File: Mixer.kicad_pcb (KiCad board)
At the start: 2 copper layers, 30 x 101 mm, 18 parts, among them J101 AudioJack2, J102 AudioJack2, J103 AudioJack2, J104 AudioJack2, J105 Conn_02x05_Counter_Clockwise, U101 TL072

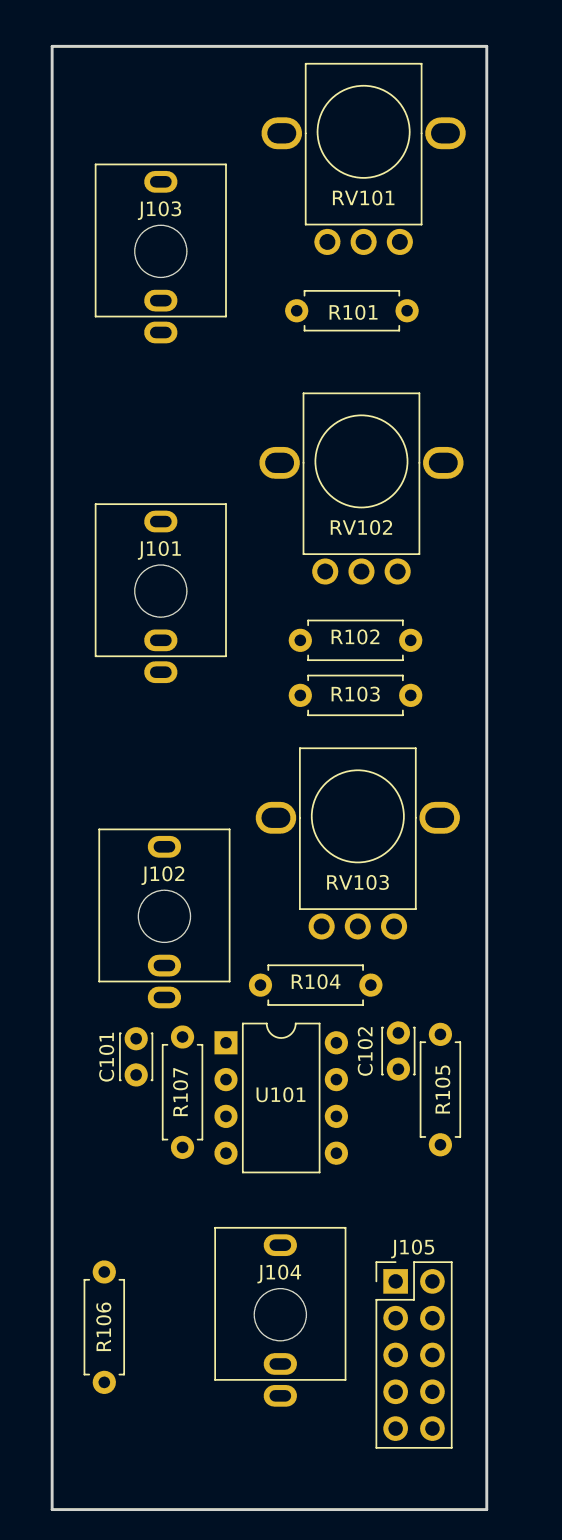
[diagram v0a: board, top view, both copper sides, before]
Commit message: Added attenuverters
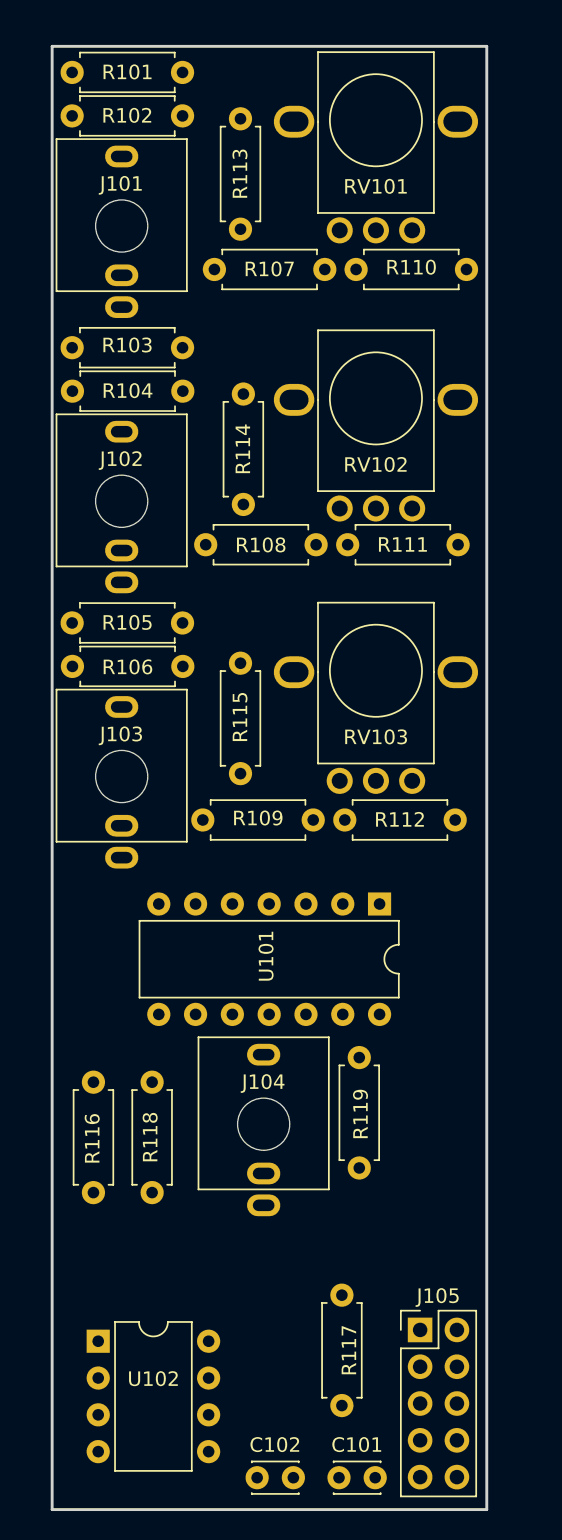
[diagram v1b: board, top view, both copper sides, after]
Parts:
- added R108: 100k, Resistor_THT:R_Axial_DIN0207_L6.3mm_D2.5mm_P7.62mm_Horizontal, F.Cu at (160.2, 104.4)
- added R109: 100k, Resistor_THT:R_Axial_DIN0207_L6.3mm_D2.5mm_P7.62mm_Horizontal, F.Cu at (160.0, 123.4)
- added R110: 100k, Resistor_THT:R_Axial_DIN0207_L6.3mm_D2.5mm_P7.62mm_Horizontal, F.Cu at (163.0, 85.4)
- added R111: 100k, Resistor_THT:R_Axial_DIN0207_L6.3mm_D2.5mm_P7.62mm_Horizontal, F.Cu at (170.0, 104.4)
- added R112: 100k, Resistor_THT:R_Axial_DIN0207_L6.3mm_D2.5mm_P7.62mm_Horizontal, F.Cu at (169.8, 123.4)
- added R113: 100k, Resistor_THT:R_Axial_DIN0207_L6.3mm_D2.5mm_P7.62mm_Horizontal, F.Cu at (155.0, 82.6)
- added R114: 100k, Resistor_THT:R_Axial_DIN0207_L6.3mm_D2.5mm_P7.62mm_Horizontal, F.Cu at (155.2, 101.6)
- added R115: 100k, Resistor_THT:R_Axial_DIN0207_L6.3mm_D2.5mm_P7.62mm_Horizontal, F.Cu at (155.0, 112.6)
- added R116: 100k, Resistor_THT:R_Axial_DIN0207_L6.3mm_D2.5mm_P7.62mm_Horizontal, F.Cu at (144.8, 149.1)
- added R117: 100k, Resistor_THT:R_Axial_DIN0207_L6.3mm_D2.5mm_P7.62mm_Horizontal, F.Cu at (162.0, 163.8)
- added R118: 100k, Resistor_THT:R_Axial_DIN0207_L6.3mm_D2.5mm_P7.62mm_Horizontal, F.Cu at (148.9, 149.1)
- added R119: 1k, Resistor_THT:R_Axial_DIN0207_L6.3mm_D2.5mm_P7.62mm_Horizontal, F.Cu at (163.2, 139.8)
- added U102: TL072, Package_DIP:DIP-8_W7.62mm, F.Cu at (145.2, 159.4)
- R101, R102, R103, R104, R105: value 100k -> 10k
- R106: value 330 -> 10k
- U101: value TL072 -> TL074; footprint Package_DIP:DIP-8_W7.62mm -> Package_DIP:DIP-14_W7.62mm
- moved R107 53.9 mm to (160.8, 85.4), turned to 180 degrees
- moved R106 49.7 mm to (151.0, 112.8), turned to 180 degrees
- moved R105 44.1 mm to (143.4, 109.8), turned to 0 degrees
- moved R104 43.0 mm to (151.0, 93.8)
- moved R102 39.5 mm to (143.4, 74.8)
- moved J103 36.4 mm to (146.8, 126.0)
- moved C101 33.4 mm to (161.8, 168.8), turned to 0 degrees
- moved C102 29.8 mm to (156.2, 168.8), turned to 0 degrees
- moved J102 28.8 mm to (146.8, 107.0)
- moved R103 28.7 mm to (143.4, 90.8)
- moved J101 25.3 mm to (146.8, 88.0)
- moved R101 22.6 mm to (143.4, 71.8)
- moved U101 14.3 mm to (164.6, 129.2), turned to 270 degrees
- moved J104 13.2 mm to (156.6, 150.0)
- moved RV103 10.1 mm to (164.3, 120.7)
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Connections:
- R101 pad 1: Net-(C101-Pad2) -> Net-(J101-PadT)
- R102 pad 1: Net-(C101-Pad2) -> Net-(R101-Pad2)
- R102 pad 2: Net-(R102-Pad2) -> GND
- R103 pad 1: Net-(C101-Pad2) -> Net-(J102-PadT)
- R104 pad 1: Net-(C102-Pad2) -> Net-(R103-Pad2)
- R104 pad 2: Net-(C101-Pad1) -> GND
- R105 pad 1: Net-(C102-Pad1) -> Net-(J103-PadT)
- R105 pad 2: Net-(C102-Pad2) -> Net-(R105-Pad2)
- R106 pad 1: Net-(J104-PadT) -> Net-(R105-Pad2)
- R106 pad 2: Net-(C102-Pad1) -> GND
- R107 pad 1: Net-(C101-Pad1) -> Net-(R107-Pad1)
- R107 pad 2: Net-(C101-Pad2) -> Net-(J101-PadT)
- RV101 pad 3: Net-(J103-PadT) -> Net-(J101-PadT)
- RV102 pad 2: Net-(R102-Pad2) -> Net-(R103-Pad2)
- RV102 pad 3: Net-(J101-PadT) -> Net-(J102-PadT)
- RV103 pad 2: Net-(R103-Pad2) -> Net-(R105-Pad2)
- RV103 pad 3: Net-(J102-PadT) -> Net-(J103-PadT)
- U101 pad 1: Net-(C101-Pad1) -> Net-(R110-Pad1)
- U101 pad 2: Net-(C101-Pad2) -> Net-(R107-Pad1)
- U101 pad 3: GND -> Net-(R101-Pad2)
- U101 pad 5: GND -> Net-(R103-Pad2)
- U101 pad 6: Net-(C102-Pad2) -> Net-(R108-Pad1)
- U101 pad 7: Net-(C102-Pad1) -> Net-(R111-Pad1)
- U101 pad 8: +12V -> Net-(R112-Pad1)

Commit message: 47pF caps and 100k resistors converted to SMD
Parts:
- C101, C102: footprint Capacitor_THT:C_Disc_D3.0mm_W2.0mm_P2.50mm -> Capacitor_SMD:C_0402_1005Metric
- R107, R108, R109, R110, R111, R112, R113, R114, R115, R116, R117, R118: footprint Resistor_THT:R_Axial_DIN0207_L6.3mm_D2.5mm_P7.62mm_Horizontal -> Resistor_SMD:R_0805_2012Metric
- moved R110 3.40 mm to (166.3, 86.2)

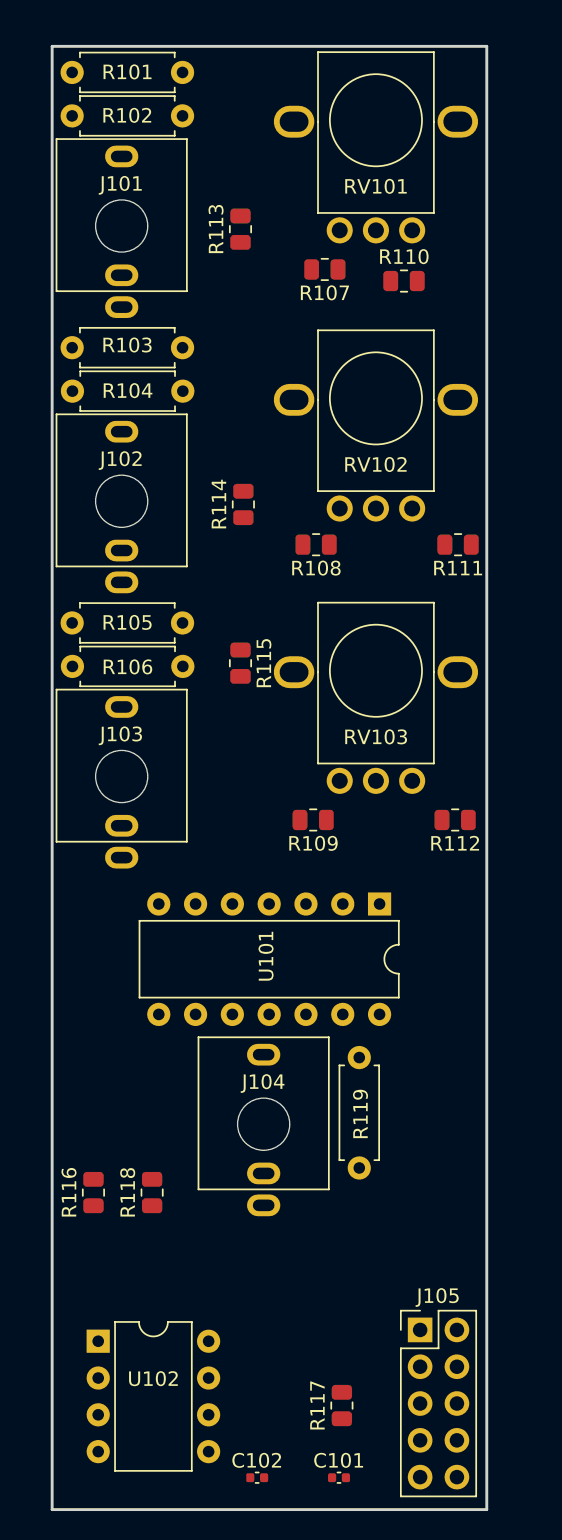
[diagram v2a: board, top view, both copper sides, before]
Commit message: fixed op amp issue
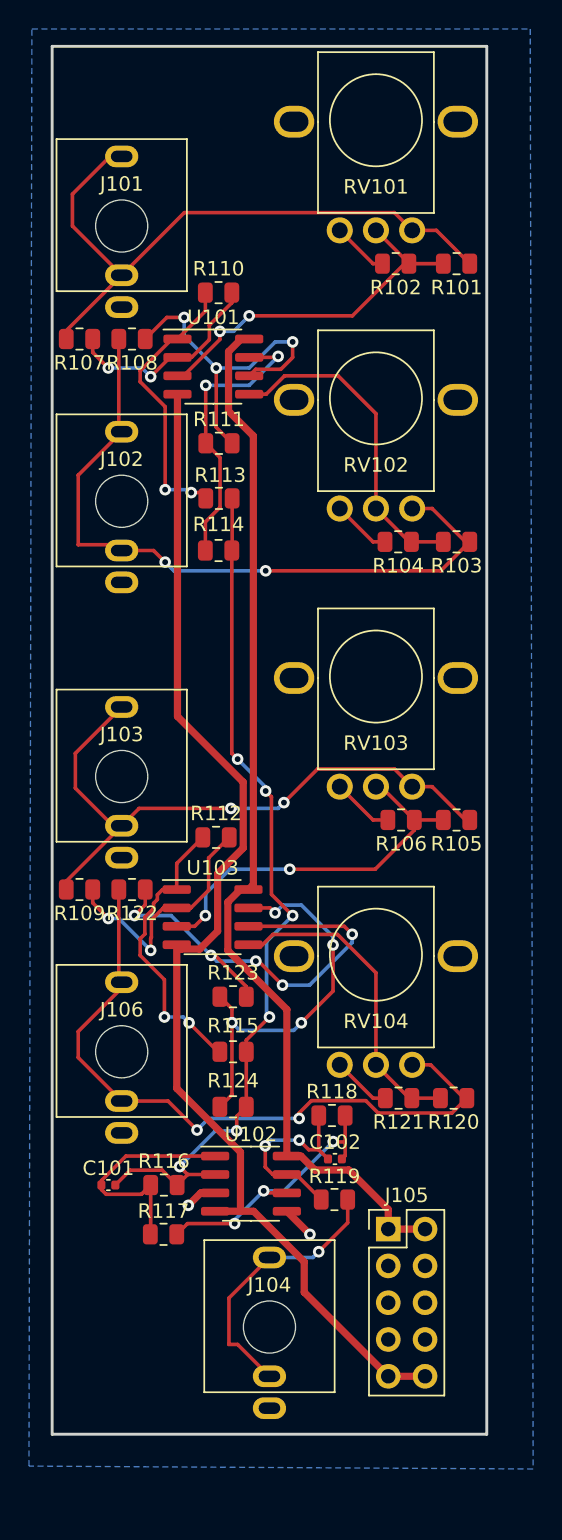
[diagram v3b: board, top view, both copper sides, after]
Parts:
- added J106: AudioJack2, A-2563:A-2563, F.Cu at (146.8, 145.0)
- added R120: 100k, Resistor_SMD:R_0805_2012Metric, F.Cu at (169.7, 142.6)
- added R121: 100k, Resistor_SMD:R_0805_2012Metric, F.Cu at (165.9, 142.6)
- added R122: 100k, Resistor_SMD:R_0805_2012Metric, F.Cu at (147.5, 128.2)
- added R123: 100k, Resistor_SMD:R_0805_2012Metric, F.Cu at (154.5, 135.6)
- added R124: 100k, Resistor_SMD:R_0805_2012Metric, F.Cu at (154.5, 143.2)
- added RV104: 100k, A-5513:A-5513, F.Cu at (164.3, 140.3)
- added U103: TL072, Package_SO:SOIC-8_3.9x4.9mm_P1.27mm, F.Cu at (153.1, 130.1)
- J105: value Conn_02x05_Counter_Clockwise -> Conn_02x05_Odd_Even
- R101, R102, R119: footprint Resistor_THT:R_Axial_DIN0207_L6.3mm_D2.5mm_P7.62mm_Horizontal -> Resistor_SMD:R_0805_2012Metric
- R103, R104: value 10k -> 22k; footprint Resistor_THT:R_Axial_DIN0207_L6.3mm_D2.5mm_P7.62mm_Horizontal -> Resistor_SMD:R_0805_2012Metric
- R105, R106: value 10k -> 47k; footprint Resistor_THT:R_Axial_DIN0207_L6.3mm_D2.5mm_P7.62mm_Horizontal -> Resistor_SMD:R_0805_2012Metric
- U101: value TL074 -> TL072; footprint Package_DIP:DIP-14_W7.62mm -> Package_SO:SOIC-8_3.9x4.9mm_P1.27mm
- U102: footprint Package_DIP:DIP-8_W7.62mm -> Package_SO:SOIC-8_3.9x4.9mm_P1.27mm
- moved U101 38.8 mm to (153.1, 92.1), turned to 0 degrees
- moved R105 29.8 mm to (169.9, 123.4), turned to 180 degrees
- moved R103 29.7 mm to (169.9, 104.2), turned to 180 degrees
- moved R101 29.6 mm to (169.9, 85.0), turned to 180 degrees
- moved R115 26.8 mm to (154.5, 139.4), turned to 180 degrees
- moved C101 25.7 mm to (145.9, 148.6)
- moved R102 24.6 mm to (165.7, 85.0), turned to 180 degrees
- moved C102 22.6 mm to (161.5, 146.8)
- moved R108 19.1 mm to (147.5, 90.2)
- moved R113 18.6 mm to (153.5, 101.2), turned to 180 degrees
- moved R106 18.4 mm to (166.1, 123.4)
- moved R104 18.1 mm to (165.9, 104.2)
- moved R111 17.9 mm to (153.5, 97.4), turned to 0 degrees
- moved R107 17.6 mm to (143.9, 90.2)
- moved R117 17.1 mm to (149.7, 152.0), turned to 180 degrees
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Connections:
- J105 pad 10: +12V -> -12V
- J105 pad 2: GND -> +12V
- J105 pad 5: -12V -> GND
- J105 pad 6: -12V -> GND
- J105 pad 9: GND -> -12V
- U101 pad 8: Net-(R112-Pad1) -> +12V
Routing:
- net -12V: track 0.00 -> 83.8 mm
- net +12V: track 0.00 -> 73.2 mm
- net Net-(C101-Pad2): track 0.00 -> 61.0 mm, vias 0 -> 6
- net Net-(J102-PadT): track 0.00 -> 49.1 mm, vias 0 -> 2
- net Net-(J106-PadT): track 0.00 -> 48.4 mm, vias 0 -> 2
- net Net-(J101-PadT): track 0.00 -> 44.7 mm
- net Net-(J103-PadT): track 0.00 -> 44.3 mm, vias 0 -> 2
- net Net-(R122-Pad1): track 0.00 -> 32.3 mm, vias 0 -> 5
- net Net-(R123-Pad1): track 0.00 -> 27.5 mm, vias 0 -> 4
- net Net-(R105-Pad2): track 0.00 -> 26.3 mm, vias 0 -> 2
- net Net-(R101-Pad2): track 0.00 -> 25.1 mm, vias 0 -> 2
- net Net-(R108-Pad1): track 0.00 -> 24.0 mm, vias 0 -> 3
- net Net-(R103-Pad2): track 0.00 -> 22.5 mm
- net Net-(R120-Pad2): track 0.00 -> 21.9 mm
- net GND: track 0.00 -> 20.8 mm, vias 0 -> 2
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- added copper zone on B.Cu, net GND
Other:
- board size 30 x 101 mm -> 30 x 95.8 mm
- board text added: "+12v"
- board text added: "-12v"
- board text added: "JLCJLCJLCJLC"
- board text added: "gnd"
- board text added: "mixer attenuverter v2 chris defrancisci"
- board text added: "stripe"
